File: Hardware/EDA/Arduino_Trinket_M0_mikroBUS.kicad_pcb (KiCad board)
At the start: 2 copper layers, 38.1 x 69.8 mm, 36 parts, among them J1 HEADER_F_2.54MM_1R8P_ST_AU_PTH, J2 HEADER_F_2.54MM_1R8P_ST_AU_PTH, J3 HEADER_F_2.54MM_1R5P_ST_AU_PTH, J4 HEADER_F_2.54MM_1R5P_ST_AU_PTH, M1 FID, M2 FID, M3 FID, P1 HEADER_M_2.54MM_1R4P_ST_AU_PTH, P2 HEADER_M_2.54MM_1R4P_ST_AU_PTH, P3 HEADER_M_2.54MM_1R4P_ST_AU_PTH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

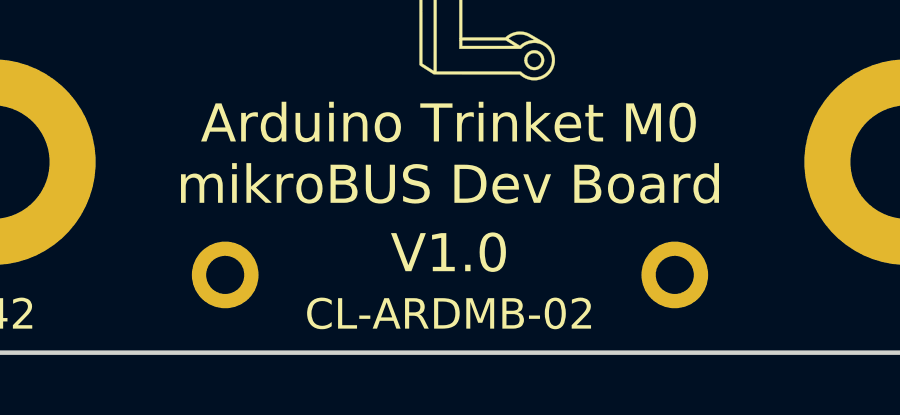
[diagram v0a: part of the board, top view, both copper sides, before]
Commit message: Corrected mistake in silkscreen artwork and regenerated PCB render image and gerbers.
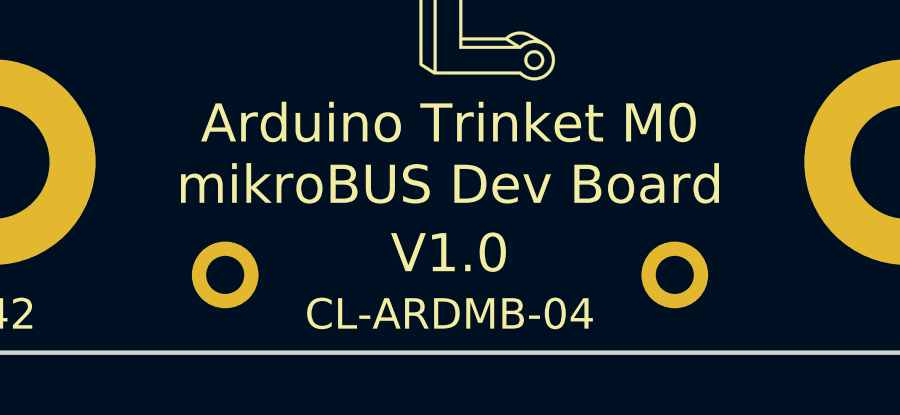
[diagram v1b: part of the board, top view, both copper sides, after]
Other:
- board text added: "CL-ARDMB-04"
- board text removed: "CL-ARDMB-02"
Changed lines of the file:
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@@
     (links 67)
     (no_connects 0)
-    (area 60.884999 31.674999 99.135001 101.675001)
+    (area 45.184287 23.97 111.025715 109.380001)
     (thickness 1.6)
     (drawings 27)
@@
   )
   (gr_line (start 72.39 82.55) (end 87.63 82.55) (angle 90) (layer F.SilkS) (width 0.127))
-  (gr_text CL-ARDMB-02 (at 80.01 100.33) (layer F.SilkS)
+  (gr_text CL-ARDMB-04 (at 80.01 100.33) (layer F.SilkS)
     (effects (font (size 1.016 1.016) (thickness 0.2032)))
   )
